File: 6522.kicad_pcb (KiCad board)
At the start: 2 copper layers, 130.9 x 78.2 mm, 37 parts, among them J7 AUDIO_OUT, P1 A2Bus, U1 AY-3-8910, U2 6522, U3 74LS05, U4 AY-3-8910, U5 6522

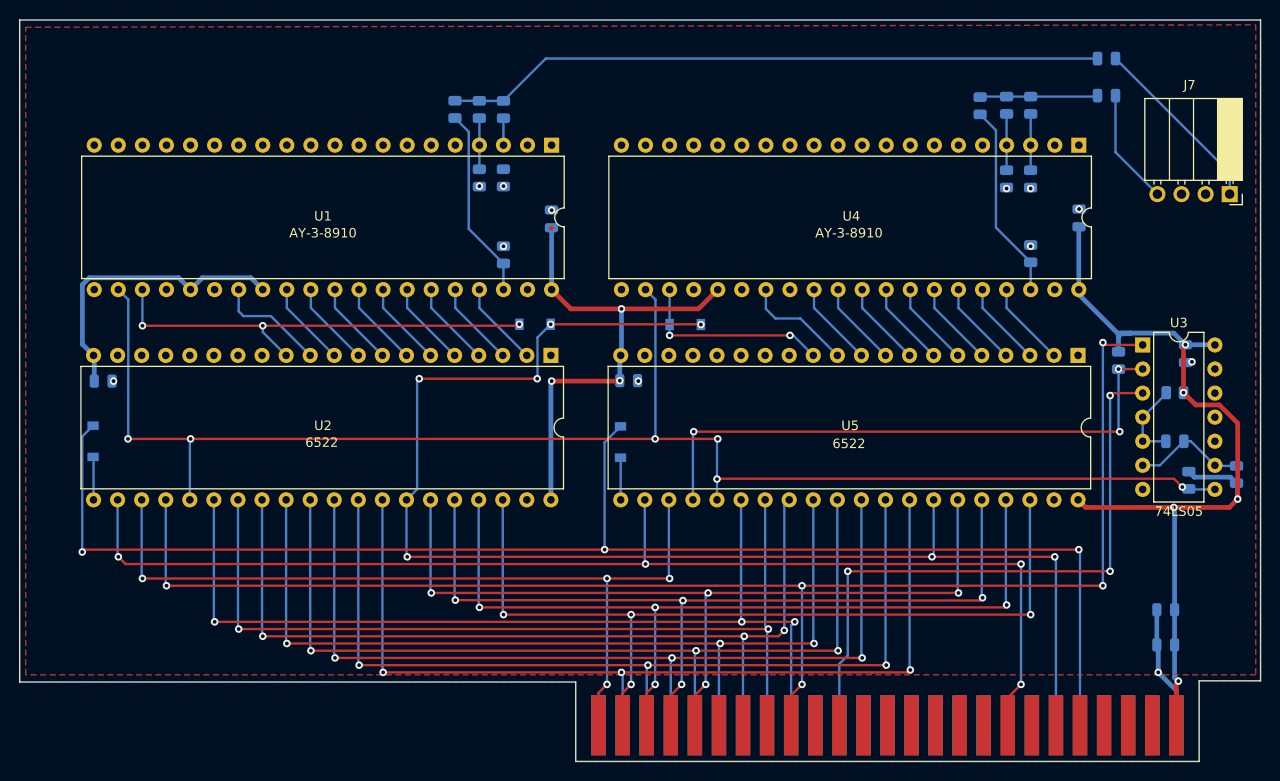
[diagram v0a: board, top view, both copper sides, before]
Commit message: All-SMD version
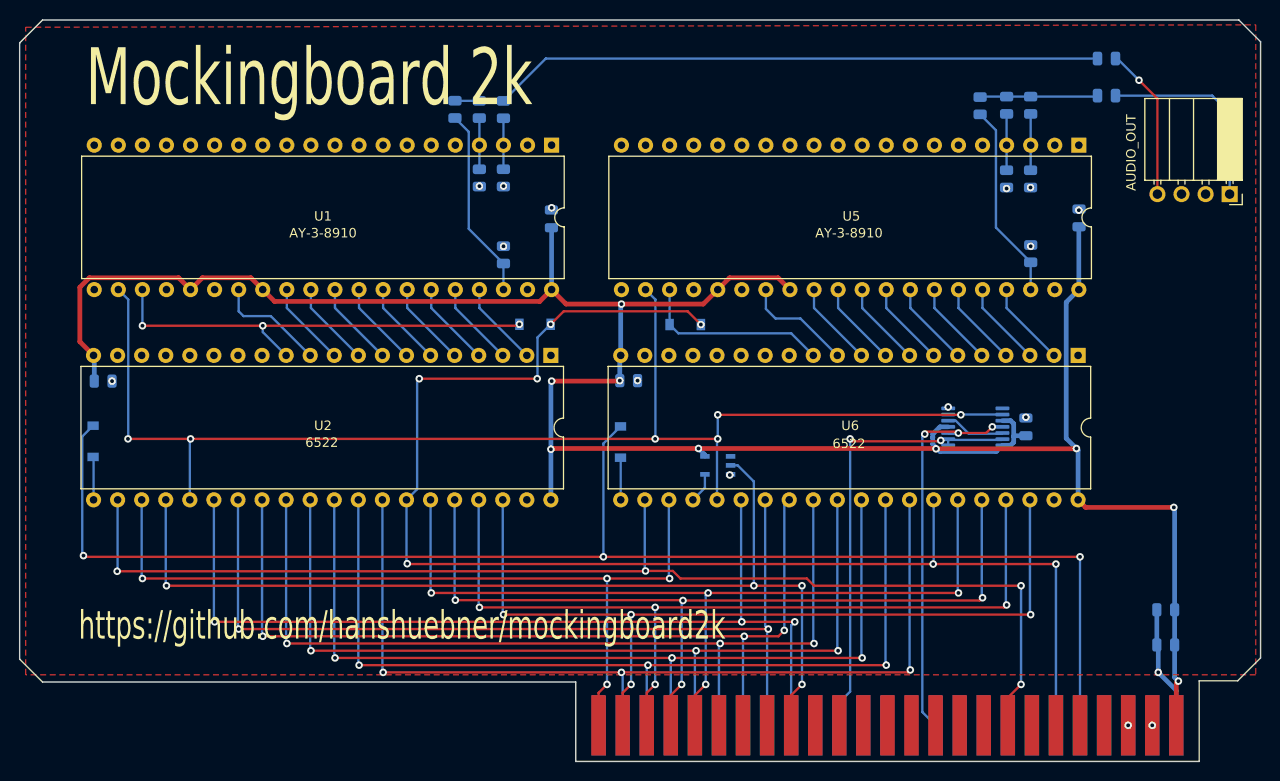
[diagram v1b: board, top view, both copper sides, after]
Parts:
- removed the C9 at (197.6, 109.5)
- removed the R10 at (199.1, 113.6)
- removed the R7 at (191.6, 100.9)
- removed the R8 at (197.6, 104.3)
- removed the R9 at (204.1, 113.0)
- added U4: 74AHCT1G04, 74ahct1g04:74AHCT1G04W5-7, B.Cu at (149.4, 112.0)
- U3: value 74LS05 -> 74HCT74; footprint Package_DIP:DIP-14_W7.62mm -> Package_SO:TSSOP-14_4.4x5mm_P0.65mm; moved to B.Cu
- moved U3 19.7 mm to (176.5, 108.0)
- moved C6 18.5 mm to (181.9, 108.0), turned to 90 degrees
- renumbered C10 to C2, C2 to C3, C3 to C4, C4 to C5, C5 to C6, C6 to C7, C7 to C8, C8 to C9, J7 to J1, R14 to R10, R15 to R11, R16 to R12, R11 to R7, R12 to R8, R13 to R9, U4 to U5, U5 to U6
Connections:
- C1 pad 2: AUDIO_R -> AUDIO_L
- C2 pad 2: AUDIO_L -> AUDIO_R
- P1 pad 36: unconnected-(P1-Pad36) -> 7M
- U3 pad 1: A7 -> PHI0
- U3 pad 10: (no net) -> VCC
- U3 pad 11: (no net) -> 7M
- U3 pad 12: (no net) -> Net-(U3-Pad12)
- U3 pad 13: (no net) -> PHI0
- U3 pad 2: Net-(R7-Pad1) -> PHI0
- U3 pad 3: PHI0 -> 7M
- U3 pad 4: Net-(C9-Pad2) -> VCC
- U3 pad 5: Net-(C9-Pad2) -> Net-(U3-Pad12)
- U3 pad 6: Net-(C9-Pad1) -> unconnected-(U3-Pad6)
- U3 pad 8: PHI2 -> unconnected-(U3-Pad8)
- U3 pad 9: Net-(C9-Pad1) -> PHI2
- U6 pad 24: Net-(R7-Pad1) -> Net-(U4-Pad4)
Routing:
- net VCC: track 179.8 -> 262.3 mm, vias 8 -> 9
- net Net-(R7-Pad1): track 61.4 -> 0.00 mm, vias 3 -> 0
- net A7: track 153.1 -> 105.5 mm, vias 5 -> 4
- net 7M: track 0.00 -> 41.3 mm, vias 0 -> 3
- net PHI2: track 160.6 -> 140.1 mm
- net PHI0: track 66.4 -> 46.2 mm, vias 3 -> 2
- net Net-(C9-Pad1): track 12.0 -> 0.00 mm
- net Net-(C9-Pad2): track 8.60 -> 0.00 mm
- net Net-(U3-Pad12): track 0.00 -> 6.33 mm
- net AUDIO_L: track 12.2 -> 16.3 mm, vias 0 -> 1
- net Net-(U4-Pad4): track 0.00 -> 3.21 mm
- net Net-(R2-Pad1): track 2.84 -> 5.39 mm
- net AUDIO_R: track 19.3 -> 21.4 mm
- net ~{RES}: track 146.3 -> 148.2 mm
- net PD2: track 20.9 -> 20.2 mm, vias 2 -> 0
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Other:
- outline, holes or cut-outs redrawn
- board text added: "GND"
- board text added: "LEFT"
- board text added: "Mockingboard 2k"
- board text added: "RIGHT"
- board text added: "https://github.com/hanshuebner/mockingboard2k"
